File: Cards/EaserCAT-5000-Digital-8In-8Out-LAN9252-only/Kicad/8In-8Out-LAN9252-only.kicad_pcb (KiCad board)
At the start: 2 copper layers, 89.2 x 58.9 mm, 98 parts, among them CN1 10pF, CN2 10pF, CN3 0.1uF, CN4 0.1uF, J1 24V Field, J10 24V_Common, J2 In5-8, J3 In1-4, J4 Output3-4, J5 Output7-8, J6 Output1-2, J7 Output5-6, J8 Conn_01x02_Pin, J9 24V_common_selector, U1 TLP292-4, U2 TLP292-4, U3 LAN9252_PT, U4 TLP292-4, U5 TLP292-4, U6 AT24CS32-SSHM, U7 AMS1117-3.3, Y1 25MHz

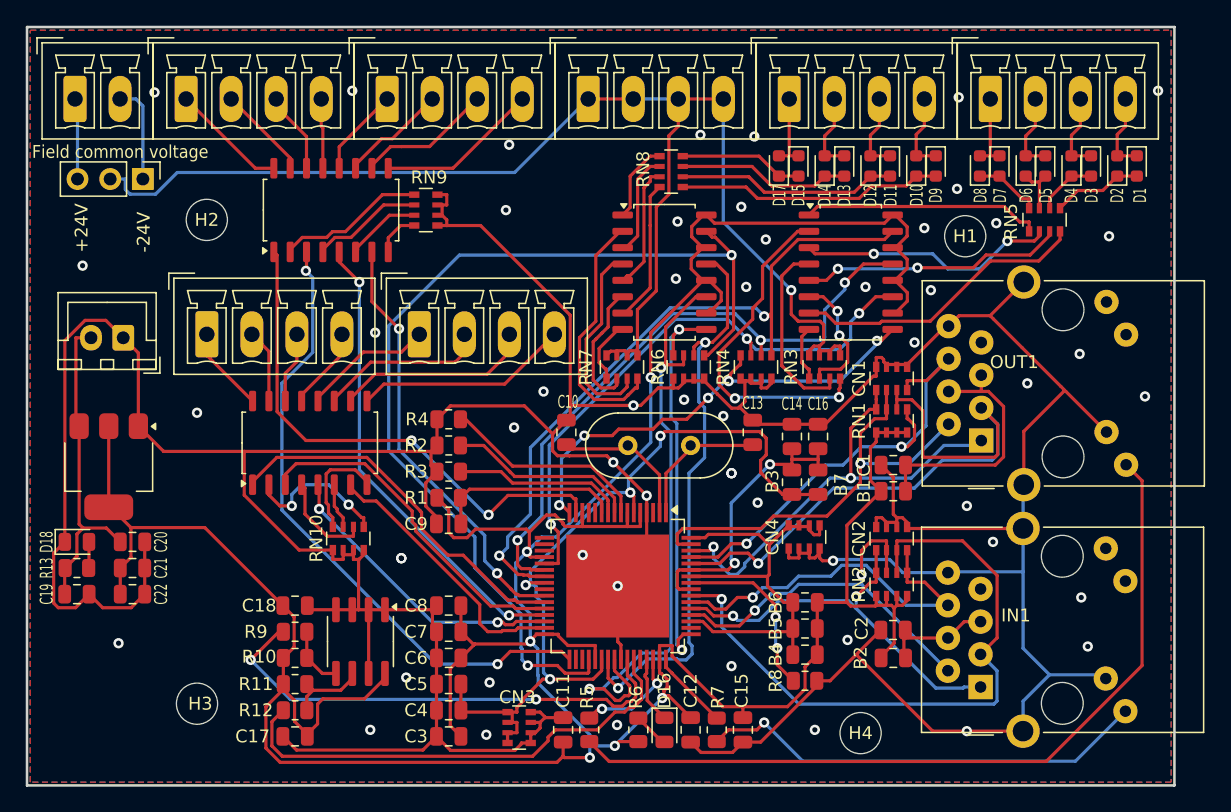
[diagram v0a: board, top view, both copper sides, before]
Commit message: Updated 24V field voltage routing. Files sent for fab
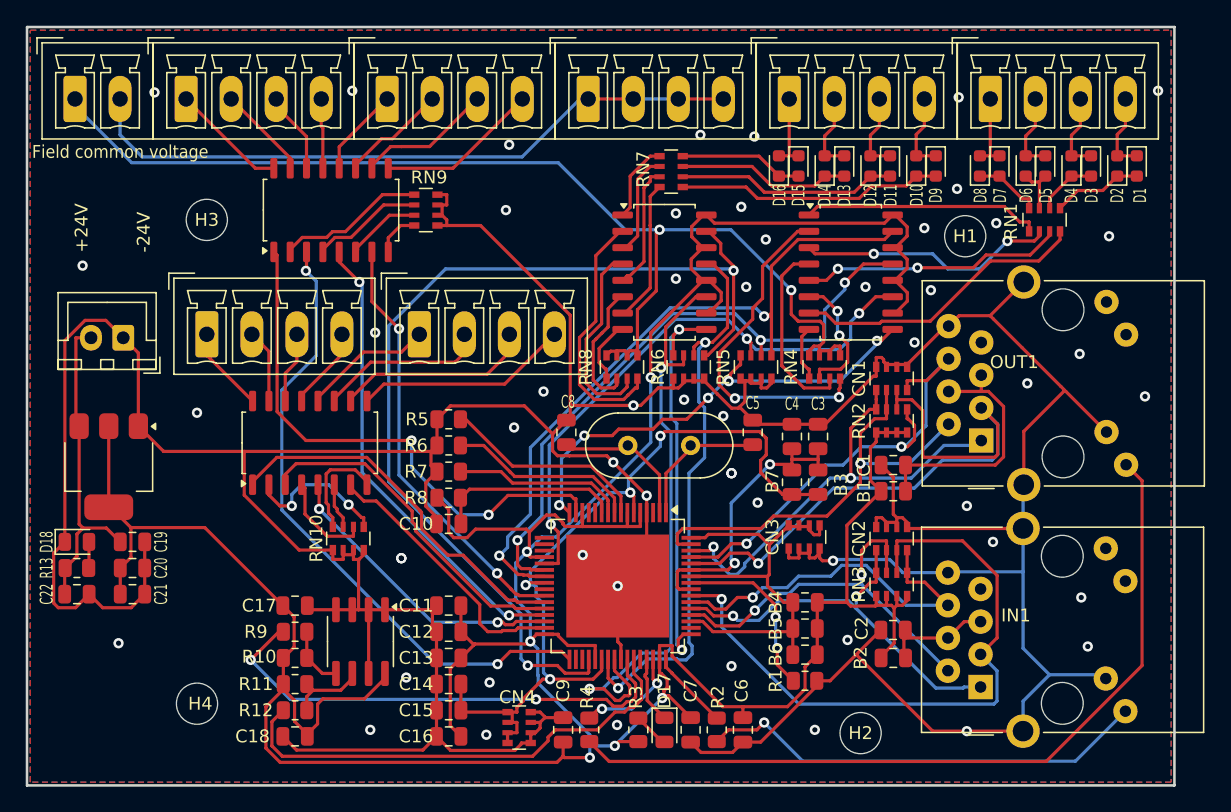
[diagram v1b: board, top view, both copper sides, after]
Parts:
- removed the J9 at (151.5, 74.3)
- renumbered B7 to B3, B6 to B4, B4 to B6, B3 to B7, C9 to C10, C8 to C11, C7 to C12, C6 to C13, C5 to C14, C4 to C15, C3 to C16, C18 to C17, C17 to C18, C20 to C19, C21 to C20, C22 to C21, C19 to C22, C16 to C3, C14 to C4, C13 to C5, C15 to C6, C12 to C7, C10 to C8, C11 to C9, CN4 to CN3, CN3 to CN4, D17 to D16, D16 to D17, H4 to H2, H2 to H3, H3 to H4, J2 to J1, J3 to J2, J10 to J3, J5 to J4, J4 to J5, J7 to J6, J6 to J7, J1 to J9, R8 to R1, R7 to R2, R6 to R3, R5 to R4, R4 to R5, R2 to R6, R3 to R7, R1 to R8, RN5 to RN1, RN1 to RN2, RN2 to RN3, RN3 to RN4, RN4 to RN5, RN8 to RN7, RN7 to RN8, U6 to U4, U4 to U5, U5 to U6
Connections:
- J3 pad 1: 24V_COMMON -> +24V_FIELD
- J3 pad 2: 24V_COMMON -> +24V_FIELD
- J3 pad 3: 24V_COMMON -> +24V_FIELD
- J3 pad 4: 24V_COMMON -> +24V_FIELD
- RN4 pad 5: 24V_COMMON -> -24V_FIELD
- RN4 pad 6: 24V_COMMON -> -24V_FIELD
- RN4 pad 7: 24V_COMMON -> -24V_FIELD
- RN4 pad 8: 24V_COMMON -> -24V_FIELD
- RN8 pad 5: 24V_COMMON -> -24V_FIELD
- RN8 pad 6: 24V_COMMON -> -24V_FIELD
- RN8 pad 7: 24V_COMMON -> -24V_FIELD
- RN8 pad 8: 24V_COMMON -> -24V_FIELD
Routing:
- net 24V_COMMON: track 104.6 -> 0.00 mm, vias 1 -> 0
- net -24V_FIELD: track 6.30 -> 87.2 mm, vias 0 -> 2
- net +24V_FIELD: track 7.68 -> 52.0 mm
- net OUT8: track 40.9 -> 42.1 mm
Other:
- board text added: "24V free polarity"
- board text added: "EaserCAT 5000: 8 In + 8 Out Digital IO MetalMusings December 2024"
- board text removed: "+24V Gnd"
- board text removed: "EaserCAT 8 In + 8 Out Digital IO MetalMusings November 2024"

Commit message: Updates to hw straps after startup of card.
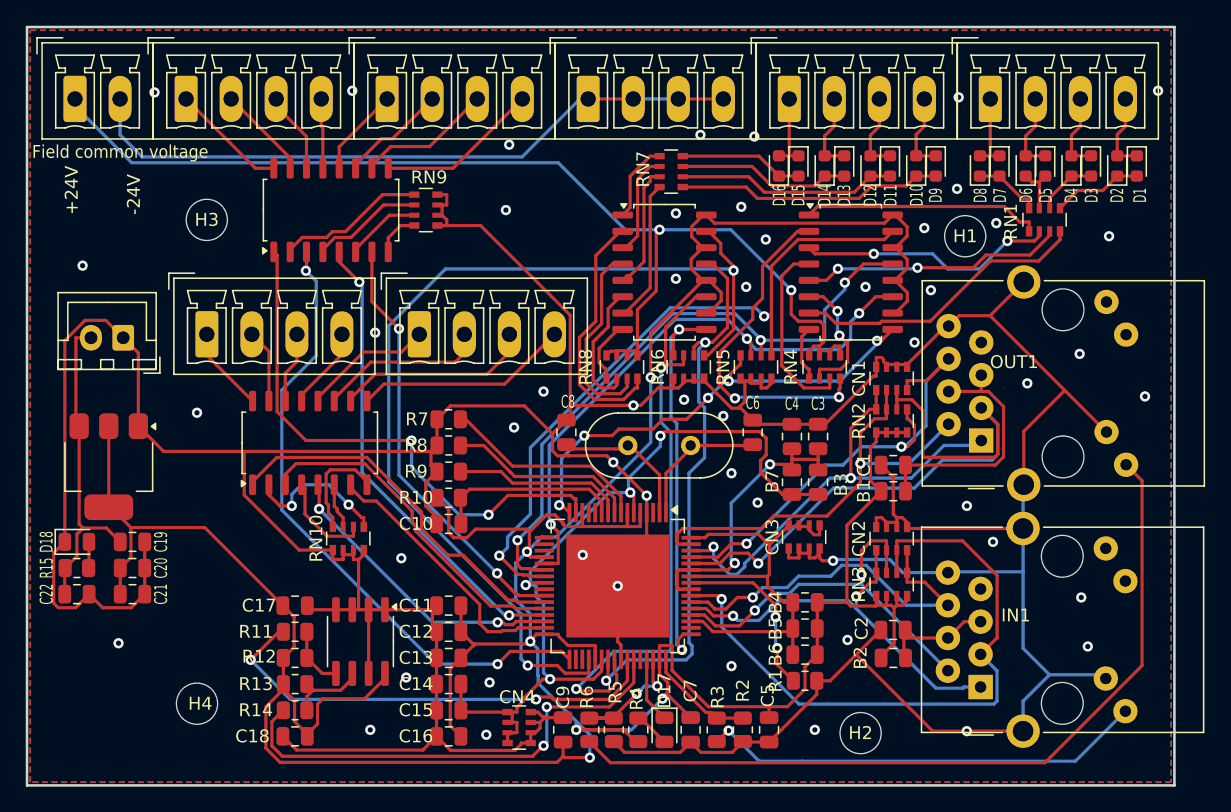
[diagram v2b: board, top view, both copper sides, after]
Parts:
- added R2: 10k, Resistor_SMD:R_0805_2012Metric, F.Cu at (198.1, 117.1)
- added R5: 10k, Resistor_SMD:R_0805_2012Metric, F.Cu at (188.1, 117.1)
- moved C5 2.03 mm to (200.2, 117.1)
- renumbered C6 to C5, C5 to C6, R8 to R10, R9 to R11, R10 to R12, R11 to R13, R12 to R14, R13 to R15, R2 to R3, R3 to R4, R4 to R6, R5 to R7, R6 to R8, R7 to R9
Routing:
- net GND: track 387.6 -> 395.3 mm, vias 55 -> 52
- net +3.3V: track 283.9 -> 289.0 mm
- net LINKACTLED0: track 6.20 -> 8.47 mm
- net LINKACTLED1: track 8.39 -> 10.4 mm
- net I2C_SDA: track 38.3 -> 36.4 mm
- net Net-(IN1-Pad9): track 35.2 -> 34.7 mm
- net I2C_SCL: track 37.5 -> 37.4 mm, vias 0 -> 2
